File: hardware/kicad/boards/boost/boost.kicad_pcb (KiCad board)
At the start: 2 copper layers, 121 x 56 mm, 11 parts, among them J1 lager ind (5V), J2 V2 ud (10V), J3 PWM (isoleret), J4 gate-forsyning, M1 IRF530, U1 4N25

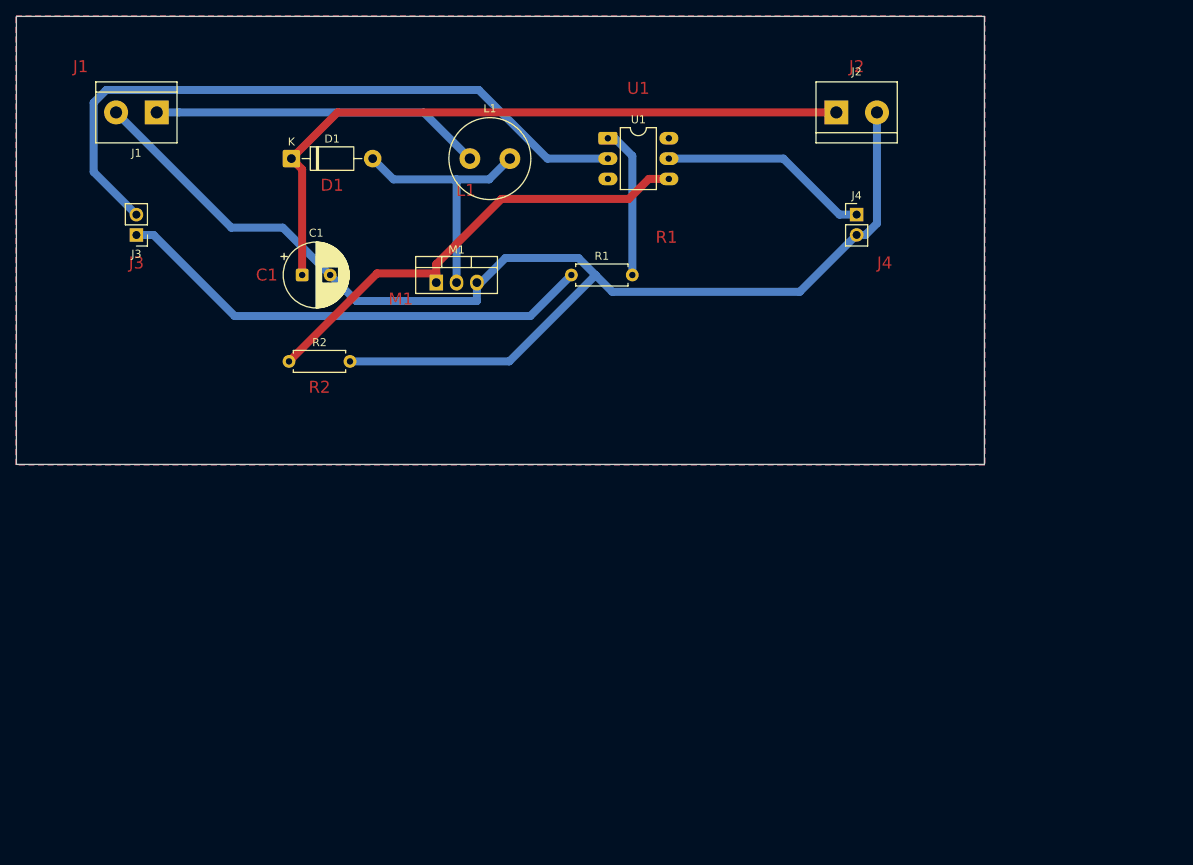
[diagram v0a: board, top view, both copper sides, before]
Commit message: Fit the measured 470uH toroid on buck/boost and fix the routing pipeline
L1 was placeholder Fastron 07P (D10/P5) - the wound toroid measures OD 34.5mm
standing on edge, legs 28.2mm c-c at 1.6mm dia. New footprint
energy_system:L_Toroid_Vertical_L34.5mm_W15.0mm_P28.20mm_LaserPads
(2.0mm drills, 4.0mm pads), boards regrown to 145x72 and rerouted
(buck 4 top tracks / boost only 2 now). Production DXF/gerbers re-exported.

Routing pipeline fixes that this flushed out:
- Set-Content -Encoding UTF8 under Windows PowerShell 5.1 writes a BOM and
  Freerouting's DSN parser chokes on it (bogus "file not found"). The stage-1
  mask now writes via [IO.File]::WriteAllText (BOM-less).
- Freerouting 2.0.1's version-check NPE can kill the SES save so jobs "hang"
  after routing; switched to the 1.9.0 jar (local CLI, same formats, Java 21).
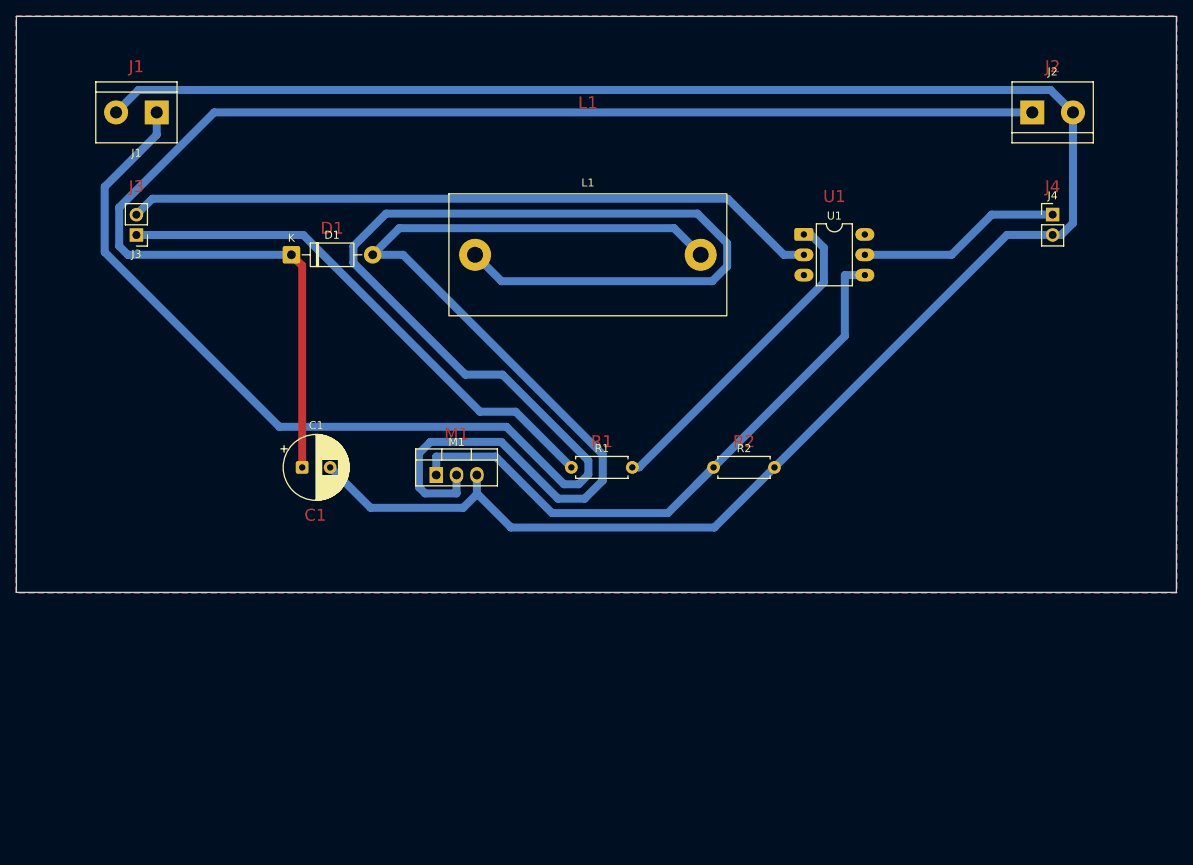
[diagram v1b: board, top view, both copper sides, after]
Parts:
- L1: footprint L_Radial_D10.0mm_P5.00mm_Fastron_07P -> L_Toroid_Vertical_L34.5mm_W15.0mm_P28.20mm_LaserPads
- moved R2 54.7 mm to (107.1, 76.4)
- moved U1 27.3 mm to (118.4, 47.3)
- moved J2 24.5 mm to (147.0, 32.0)
- moved J4 24.5 mm to (149.5, 44.8)
- moved M1 24.1 mm to (72.5, 77.3)
- moved C1 24.0 mm to (55.7, 76.4)
- moved R1 24.0 mm to (89.4, 76.4)
- moved L1 12.0 mm to (77.3, 49.8)
- moved D1 12.0 mm to (54.4, 49.8)
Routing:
- net /VIN_5V: track 41.5 -> 223.0 mm
- net Net-(D1-A): track 32.2 -> 125.1 mm
- net GND: track 163.0 -> 251.3 mm
- net /VOUT_V2: track 85.6 -> 173.0 mm
- net Net-(R1-Pad2): track 18.9 -> 41.1 mm
- net GATE: track 58.8 -> 78.6 mm
- net PWM: track 60.7 -> 66.4 mm
- net GND_MCU: track 84.7 -> 87.2 mm
- net +12V: track 26.4 -> 25.6 mm
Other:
- board size 121 x 56 mm -> 145 x 72 mm

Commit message: Move all boards to the 104x104 jig format with compact placement
The laser positioning jig takes an exactly 109x109 mm copper blank, so every
board now has identical 104x104 edge cuts (2.5 mm rim). pcb_build.py:
- fixed JIG_W/JIG_H outline, hard failure if content overflows the square
- compact packing: 5 mm bbox gaps (was 8), squarish component cluster below
  the connector zone instead of full-width rows
- mppt/current_sense PLACE layouts re-arranged for the square and tightened

All 7 boards rerouted: 0 unconnected, 0 real DRC errors, and no vias needed
anywhere (the square format routes better than the old elongated boards).
Production DXF/gerbers re-exported; README run-plan updated for the jig
(cut blanks to exactly 109x109, all boards share the same size now).
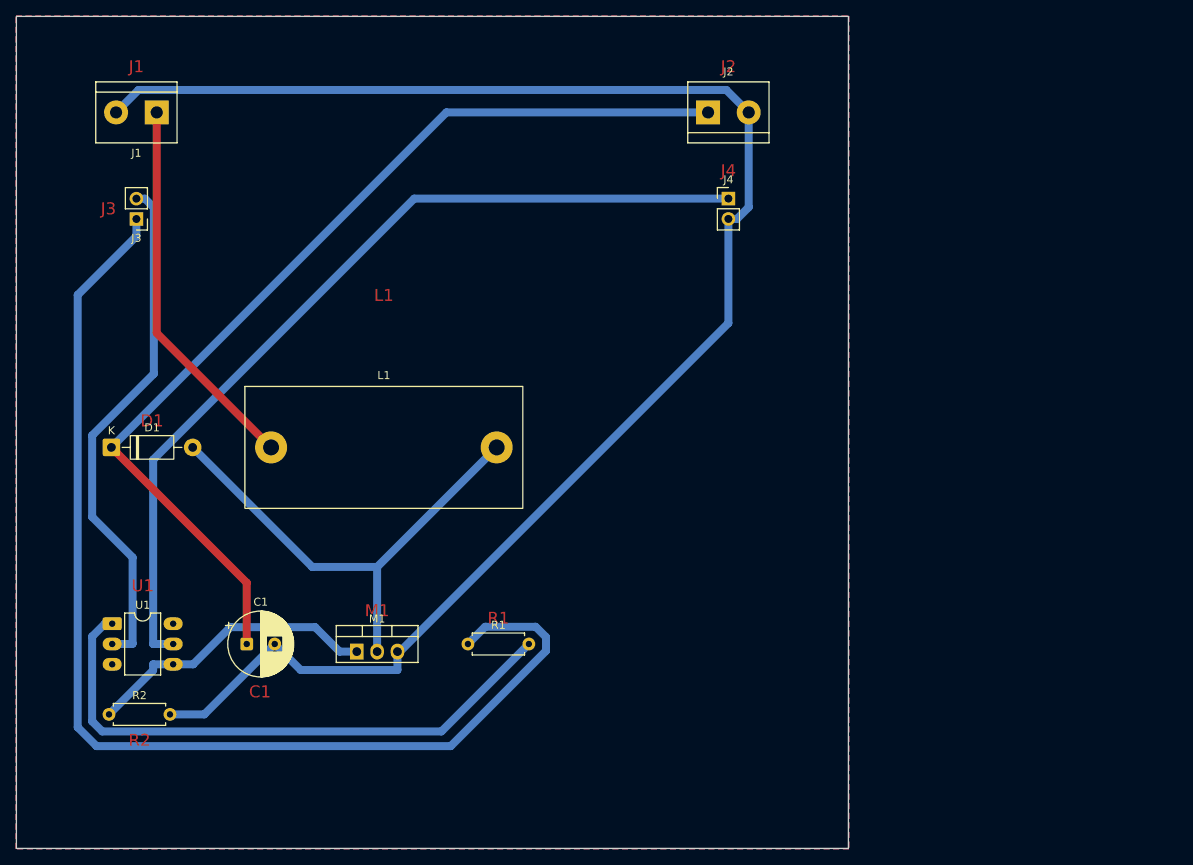
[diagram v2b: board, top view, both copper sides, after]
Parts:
- moved U1 99.2 mm to (32.0, 95.9)
- moved R2 81.6 mm to (31.6, 107.2)
- moved J4 40.6 mm to (109.0, 42.8)
- moved J2 40.5 mm to (106.5, 32.0)
- moved L1 35.1 mm to (51.8, 73.9)
- moved D1 33.0 mm to (31.9, 73.9)
- moved R1 25.6 mm to (76.4, 98.5)
- moved M1 24.2 mm to (62.5, 99.4)
- moved C1 23.1 mm to (48.8, 98.5)
- moved J3 2.00 mm to (35.0, 45.3)
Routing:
- net /VIN_5V: track 223.0 -> 47.8 mm
- net +12V: track 25.6 -> 111.0 mm
- net PWM: track 66.4 -> 143.9 mm
- net Net-(D1-A): track 125.1 -> 61.0 mm
- net /VOUT_V2: track 173.0 -> 123.5 mm
- net GND: track 251.3 -> 203.7 mm
- net GATE: track 78.6 -> 37.2 mm
- net Net-(R1-Pad2): track 41.1 -> 73.4 mm
- net GND_MCU: track 87.2 -> 65.0 mm
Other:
- board size 145 x 72 mm -> 104 x 104 mm

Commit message: Condense and center all boards in the jig outline; reroute drive_circuit
Placement (pcb_build.py): connector columns now hug the component block
instead of sitting at the board edges, and the whole cluster is translated to
the center of the 104x104 outline - nothing sits next to the edge cuts
anymore. Fail-hard check if a cluster outgrows the jig.

drive_circuit keeps the hand-made GUI placement but is rerouted with the
two-stage flow: 43 top tracks + 1 via from the GUI autoroute down to 20
pin-to-pin bridges, no via. New tools/strip_routing.py removes existing
routing textually (sexpdata) - in-process pcbnew Remove() access-violates.

All 7 boards: 0 unconnected, 0 real DRC errors, no vias anywhere; buck is
now fully single-sided (0 top tracks). Production files re-exported.
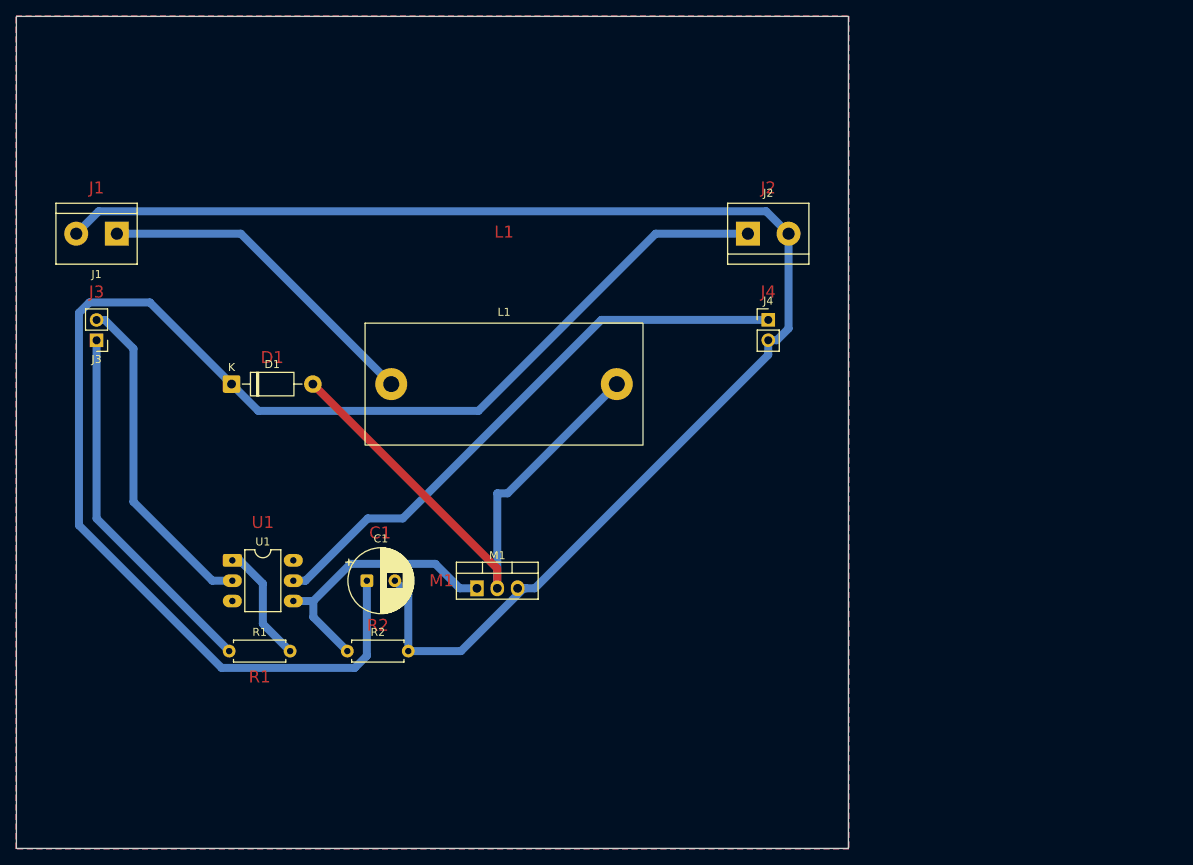
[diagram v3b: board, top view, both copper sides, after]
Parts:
- moved R2 30.8 mm to (61.4, 99.3)
- moved R1 29.9 mm to (46.6, 99.3)
- moved C1 17.0 mm to (63.8, 90.5)
- moved M1 17.0 mm to (77.6, 91.5)
- moved D1 17.0 mm to (46.9, 66.0)
- moved L1 17.0 mm to (66.9, 66.0)
- moved U1 17.0 mm to (47.0, 88.0)
- moved J2 16.0 mm to (111.4, 47.2)
- moved J4 16.0 mm to (114.0, 57.9)
- moved J1 16.0 mm to (32.6, 47.2)
- moved J3 16.0 mm to (30.0, 60.5)
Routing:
- net PWM: track 143.9 -> 45.7 mm
- net Net-(R1-Pad2): track 73.4 -> 14.9 mm
- net /VOUT_V2: track 123.5 -> 178.9 mm
- net +12V: track 111.0 -> 72.9 mm
- net GND: track 203.7 -> 178.8 mm
- net GND_MCU: track 65.0 -> 41.7 mm
- net Net-(D1-A): track 61.0 -> 67.5 mm
- net /VIN_5V: track 47.8 -> 42.1 mm
- net GATE: track 37.2 -> 34.2 mm

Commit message: Boost v2 med IR2110 gate-driver + boost test-resultater
- boost_v2: integreret IR2110 gate-drive (opto -> IR2110 -> low-side MOSFET),
  generator (build_boost_v2.py), schematic, board og laser/gerber-filer
- buck_v2: patchet til IR2110 high-side drive (patch_buck_v2_ir2110.py)
- boost: opdateret board, gamle produktions-DXF erstattet af boost_v2
- AD3 boost-bringup script (tools/ad3/boost_test.py)
- BOM opdateret med IR2110/CNY17; CNY17- og IRF530-datablade
- rapport: boost maaleresultater (10 kHz, 40%) med figur
- HANDOFF-dokument for buck/boost IR2110-redesign; PCB_RESULTS opdateret
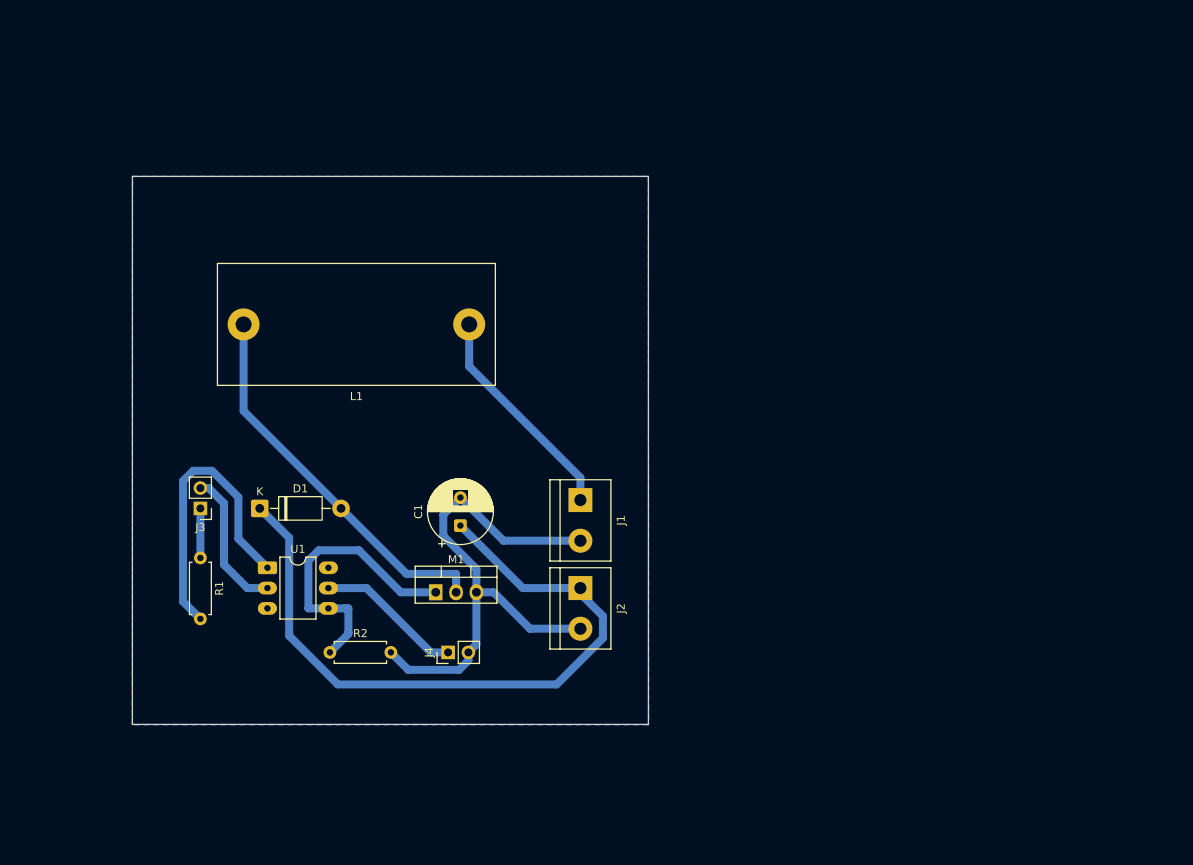
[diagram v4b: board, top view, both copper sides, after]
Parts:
- moved J1 66.8 mm to (90.5, 80.5), turned to -90 degrees
- moved J4 57.7 mm to (74.0, 99.5), turned to 90 degrees
- moved J2 49.0 mm to (90.5, 91.5), turned to -90 degrees
- moved J3 24.7 mm to (43.0, 81.5)
- moved D1 15.9 mm to (50.4, 81.5)
- moved C1 13.6 mm to (75.5, 83.7), turned to 90 degrees
- moved L1 12.3 mm to (76.6, 58.5), turned to 180 degrees
- moved R1 12.2 mm to (43.0, 87.7), turned to -90 degrees
- moved M1 5.17 mm to (72.4, 92.0)
- moved U1 4.48 mm to (51.4, 88.9)
- moved R2 2.18 mm to (59.2, 99.5)
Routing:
- net GND: track 178.8 -> 66.6 mm
- net /VOUT_V2: track 178.9 -> 87.5 mm
- net +12V: track 72.9 -> 18.3 mm
- net PWM: track 45.7 -> 6.19 mm
- net GND_MCU: track 41.7 -> 18.0 mm
- net Net-(R1-Pad2): track 14.9 -> 37.3 mm
- net Net-(D1-A): track 67.5 -> 47.1 mm
- net /VIN_5V: track 42.1 -> 26.7 mm
- net GATE: track 34.2 -> 36.1 mm
- removed copper zone on F.Cu, net (none)
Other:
- board size 104 x 104 mm -> 64.5 x 68.5 mm
- board text removed: "C1"
- board text removed: "D1"
- board text removed: "J1"
- board text removed: "J2"
- board text removed: "J3"
- board text removed: "J4"
- board text removed: "L1"
- board text removed: "M1"
- board text removed: "R1"
- board text removed: "R2"
- board text removed: "U1"
